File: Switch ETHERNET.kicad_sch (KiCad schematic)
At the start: 133 parts, among them J1 Conn_01x04, J2 RJ45_LED, J3 RJ45_LED, J4 RJ45_LED, J5 RJ45_LED, J6 RJ45_LED, J7 Jack-DC, J8 Conn_01x04, J9 Conn_01x02_Pin, Q1 SI2301-ZE, SW1 SW_Push, U1 RTL8367N-VB-CG, U2 TPS563201, U3 TPS563201, Y1 25MHz

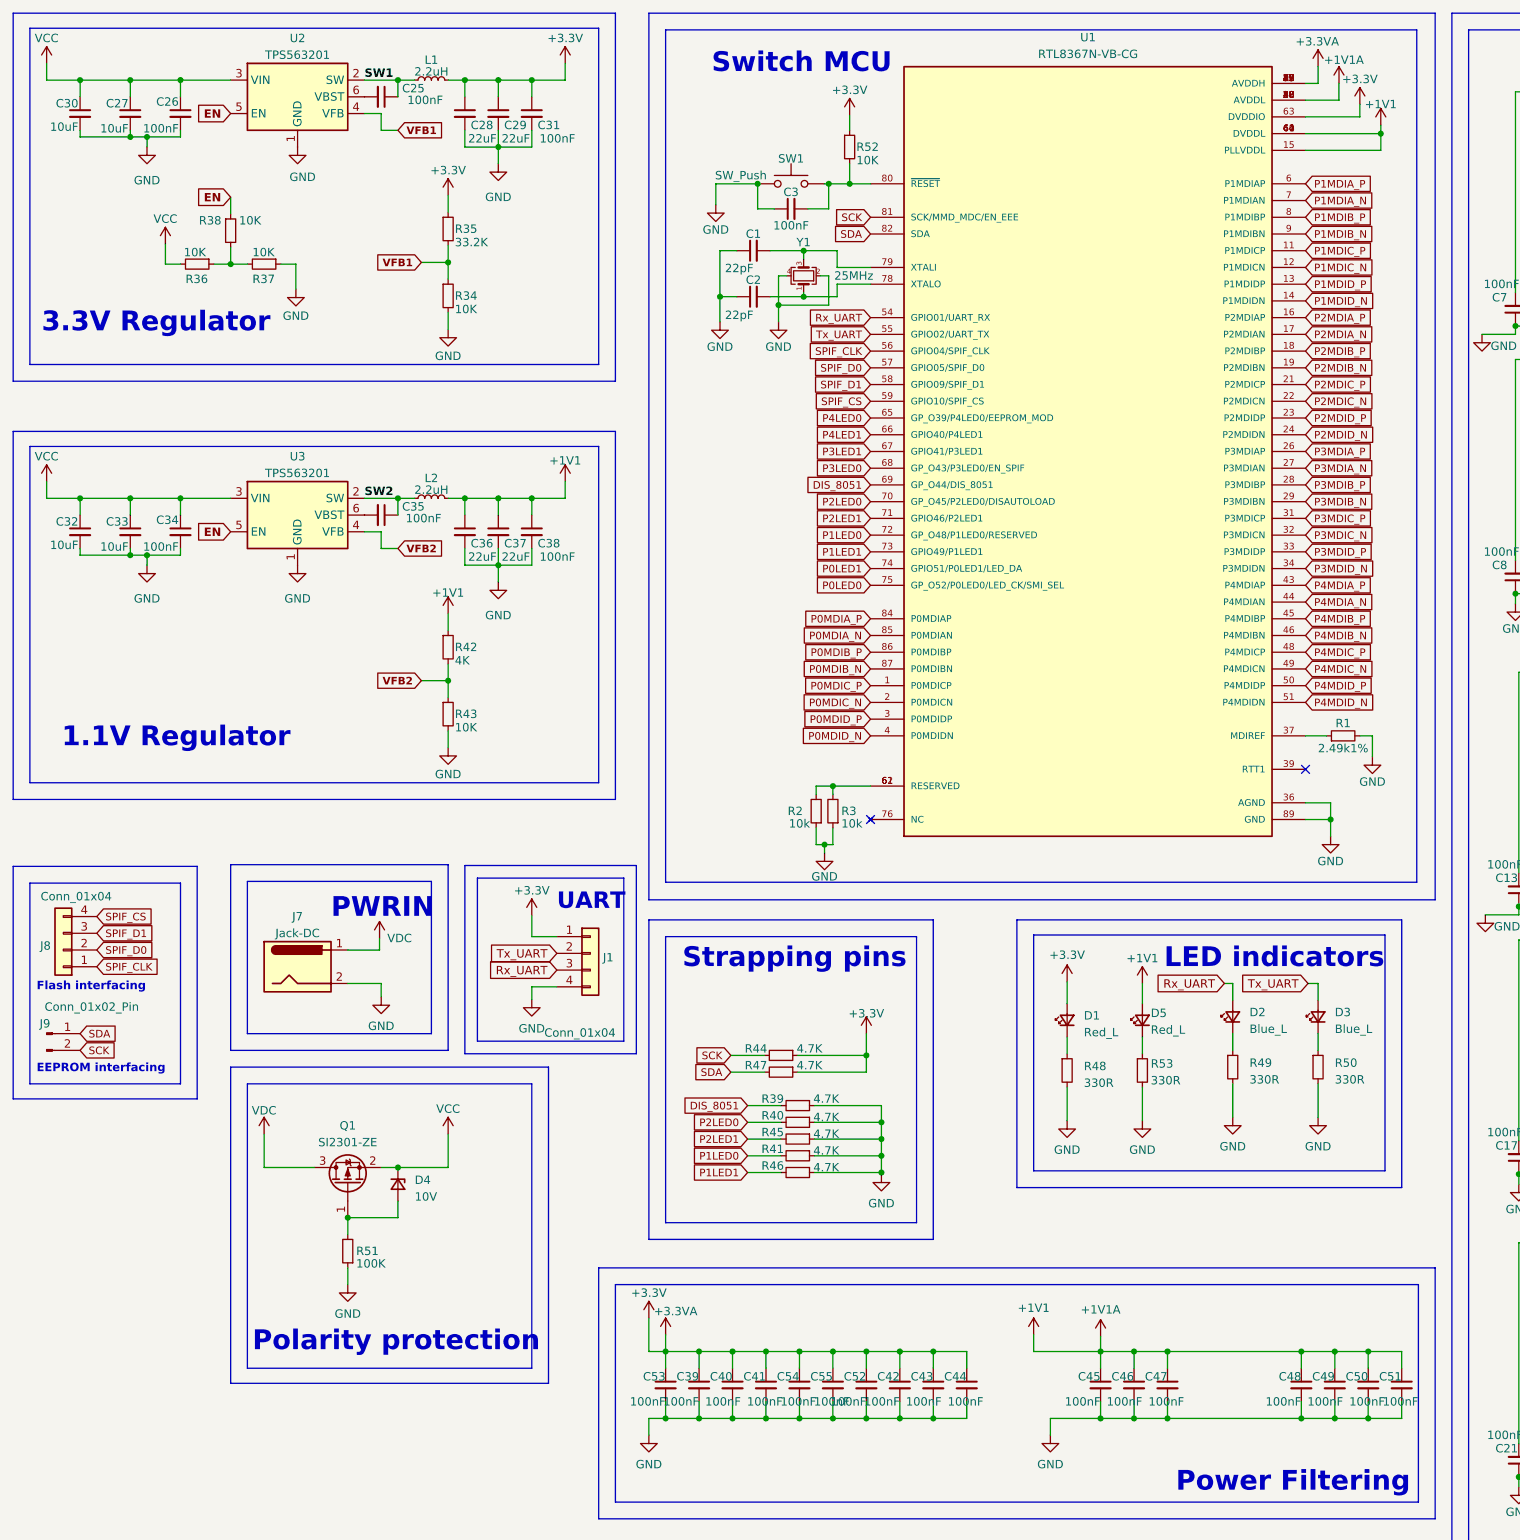
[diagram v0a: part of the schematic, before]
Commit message: Buck converters and power rails routed
I finished routing the two Buck converters and routed the power rails till the IC + placement of decoupling capacitors + in-board spaces between the analog and digital sections + routed the LEDs of the RJ-45 connectors
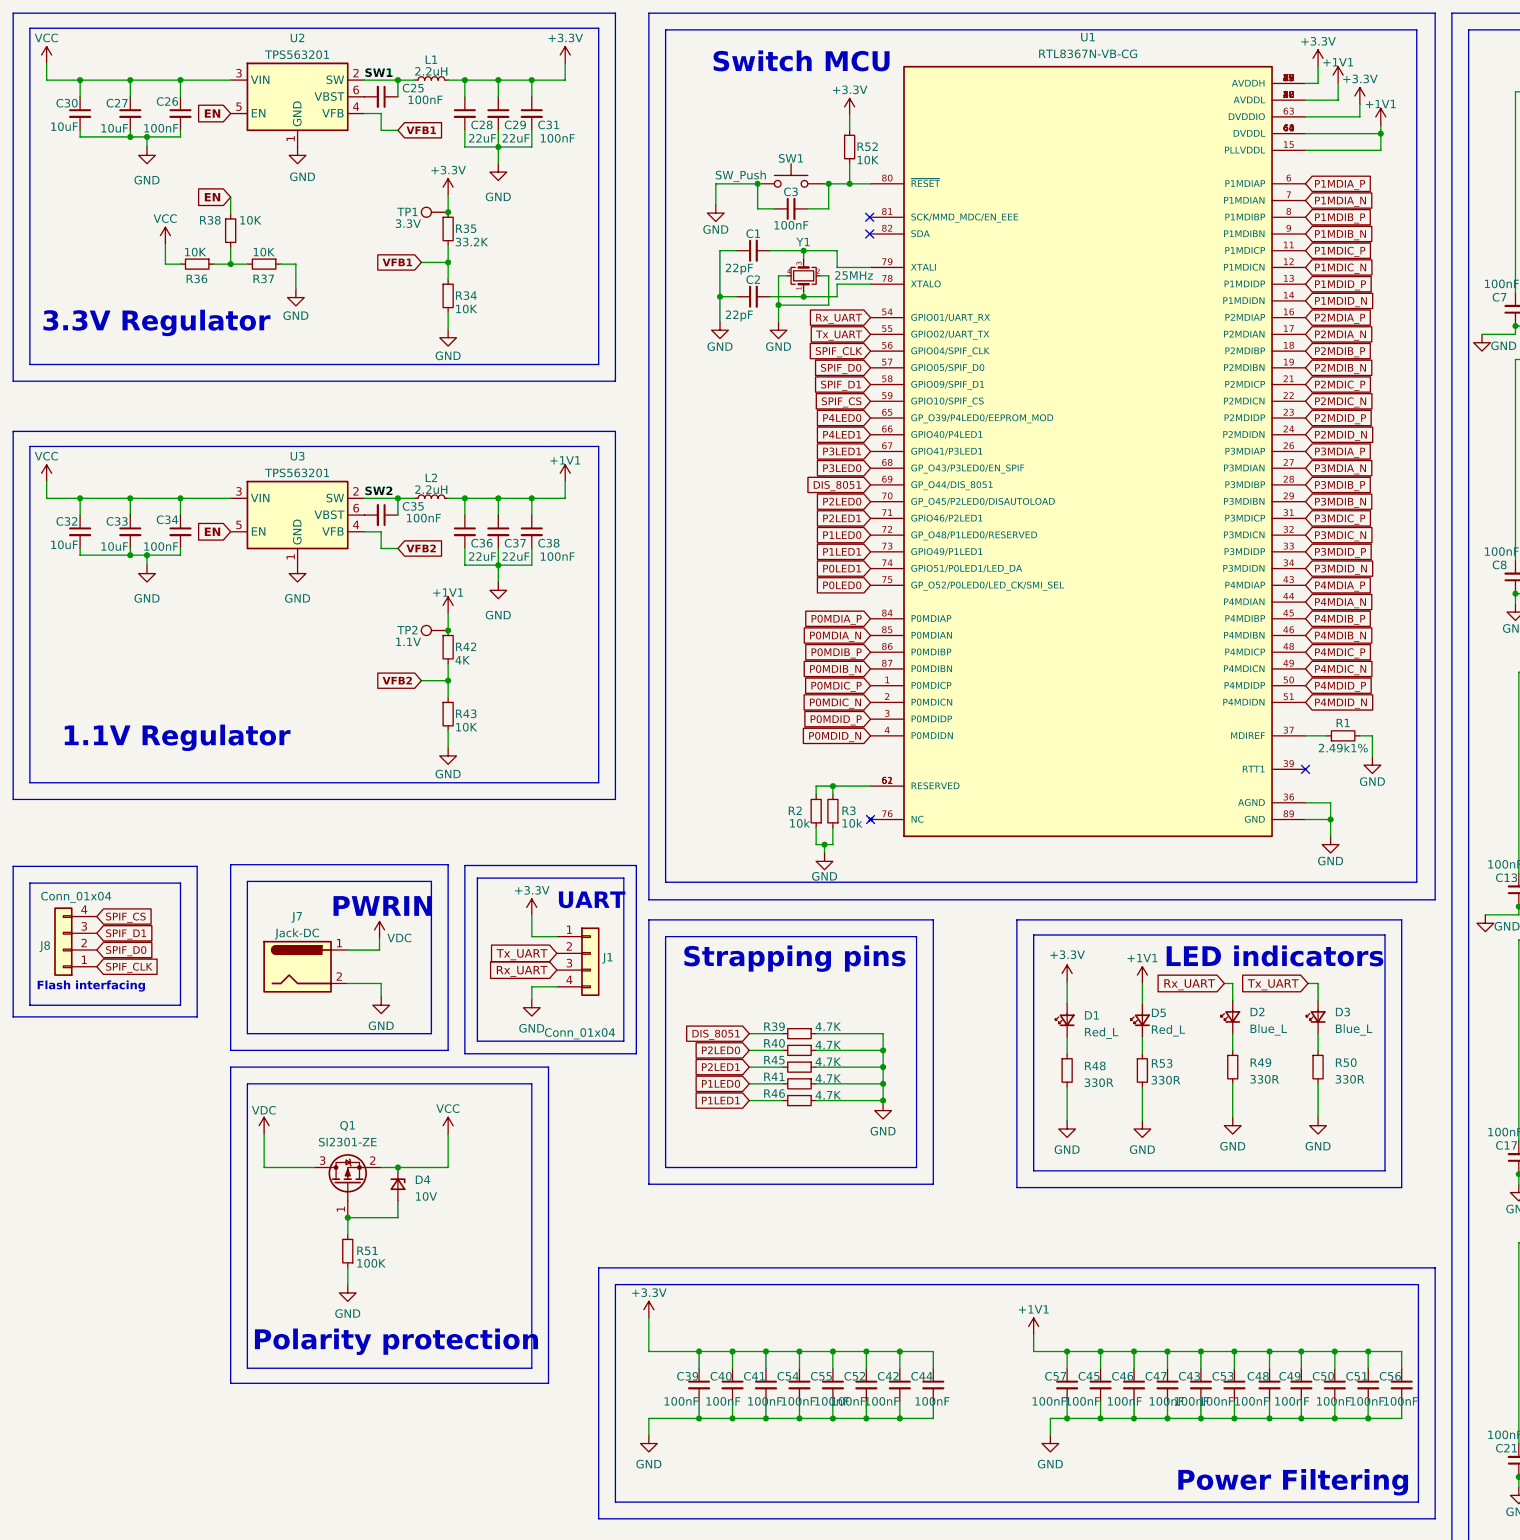
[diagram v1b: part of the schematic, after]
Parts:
- removed J9: Conn_01x02_Pin, Connector_PinHeader_2.54mm:PinHeader_1x02_P2.54mm_Vertical, symbol Connector:Conn_01x02_Pin
- removed R44, R47: 4.7K, Resistor_SMD:R_0603_1608Metric, symbol Device:R_Small
- added C56, C57: 100nF, Capacitor_SMD:C_0402_1005Metric, symbol Device:C_Small
- added TP1: 3.3V, TestPoint:TestPoint_Pad_1.0x1.0mm, symbol Connector:TestPoint
- added TP2: 1.1V, TestPoint:TestPoint_Pad_1.0x1.0mm, symbol Connector:TestPoint
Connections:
- net +1V1: now also C56.1, C57.1, TP2.1; no longer C28.1, C29.1, C31.1, C39.1, C40.1, C41.1, C42.1, C44.1, C52.1, C54.1, C55.1, D1.2 (A), J1.1 (Pin_1), L1.2, R35.1, R52.1, U1.25 (AVDDH), U1.35 (AVDDH), U1.40 (AVDDH), U1.42 (AVDDH), U1.5 (AVDDH), U1.52 (AVDDH), U1.63 (DVDDIO), U1.77 (AVDDH), U1.83 (AVDDH)
- net GND: now also C56.2, C57.2
- net SCK: no longer names the net of U1.81 (SCK/MMD_MDC/EN_EEE)
- net SDA: no longer names the net of U1.82 (SDA)
- new net +3.3V: C28.1, C29.1, C31.1, C39.1, C40.1, C41.1, C42.1, C44.1, C52.1, C54.1, C55.1, D1.2 (A), J1.1 (Pin_1), L1.2, R35.1, R52.1, TP1.1, U1.25 (AVDDH), U1.35 (AVDDH), U1.40 (AVDDH), U1.42 (AVDDH), U1.5 (AVDDH), U1.52 (AVDDH), U1.63 (DVDDIO), U1.77 (AVDDH), U1.83 (AVDDH)
- no-connect marks 2 -> 4
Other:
- note removed: "EEPROM interfacing"
- moved on the sheet: C44, C48, C49, C50, C51, C53, R39, R40, R41, R45, R46

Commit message: Added Photos of PCB in real life
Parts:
- removed J7: Jack-DC, Connector_BarrelJack:BarrelJack_Wuerth_6941xx301002, symbol Connector:Jack-DC
- added H1, H2, H3: MountingHole, MountingHole:MountingHole_2.7mm_M2.5_Pad_Via, symbol Mechanical:MountingHole
- added J7: Barrel_Jack_Switch, Connector_BarrelJack:BarrelJack_Horizontal, symbol Connector:Barrel_Jack_Switch
- J2, J3, J4, J5, J6: symbol Connector:RJ45_LED -> Connector:RJ45_LED_Shielded_x2
- R10, R11, R12, R13, R14, R15, R16, R17, R18, R19, R20, R21, R22, R23, R4, R5, R6, R7, R8, R9: footprint Resistor_SMD:R_0201_0603Metric -> Resistor_SMD:R_0402_1005Metric
- T1: renamed from TR1; footprint H4801G:H4801G -> Components:H4801G
- T2: renamed from TR2; footprint H4801G:H4801G -> Components:H4801G
- renumbered TR3 to T3
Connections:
- net +1V1: no longer C43.1, C45.1, C46.1, C47.1, C50.1, C51.1, C56.1, U1.10 (AVDDL), U1.20 (AVDDL), U1.30 (AVDDL), U1.38 (AVDDL), U1.47 (AVDDL), U1.53 (AVDDL), U1.88 (AVDDL)
- net +3.3V: no longer C31.1, C39.1, C41.1, C42.1, C44.1, C52.1, C54.1, C55.1, U1.25 (AVDDH), U1.35 (AVDDH), U1.40 (AVDDH), U1.42 (AVDDH), U1.5 (AVDDH), U1.52 (AVDDH), U1.77 (AVDDH), U1.83 (AVDDH)
- net Earth: now also J2.SH, J3.SH, J4.SH, J5.SH, J6.SH
- net GND: now also J7.2, J7.3
- net VDC: now also J7.1
- new net +1.1VA: C43.1, C45.1, C46.1, C47.1, C50.1, C51.1, C56.1, U1.10 (AVDDL), U1.20 (AVDDL), U1.30 (AVDDL), U1.38 (AVDDL), U1.47 (AVDDL), U1.53 (AVDDL), U1.88 (AVDDL)
- new net +3.3VA: C31.1, C39.1, C41.1, C42.1, C44.1, C52.1, C54.1, C55.1, U1.25 (AVDDH), U1.35 (AVDDH), U1.40 (AVDDH), U1.42 (AVDDH), U1.5 (AVDDH), U1.52 (AVDDH), U1.77 (AVDDH), U1.83 (AVDDH)
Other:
- note added: "12/6/2023"
- note added: "ETHERNET Switch"
- note added: "Omar Fayed"
- moved on the sheet: C31, C39, C40, C41, C42, C43, C44, C45, C46, C47, C48, C49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
